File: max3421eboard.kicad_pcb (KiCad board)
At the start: 2 copper layers, 41.3 x 48.9 mm, 28 parts, among them J1 USB A, J2 USB MicroB, J3 1x10, J4 1x8, J5 1x8, J6 1x3, J7 Conn_01x04, U1 MAX3421E, U2 LP2985-3.3, U3 STMPS2141STR, Y1 12MHz

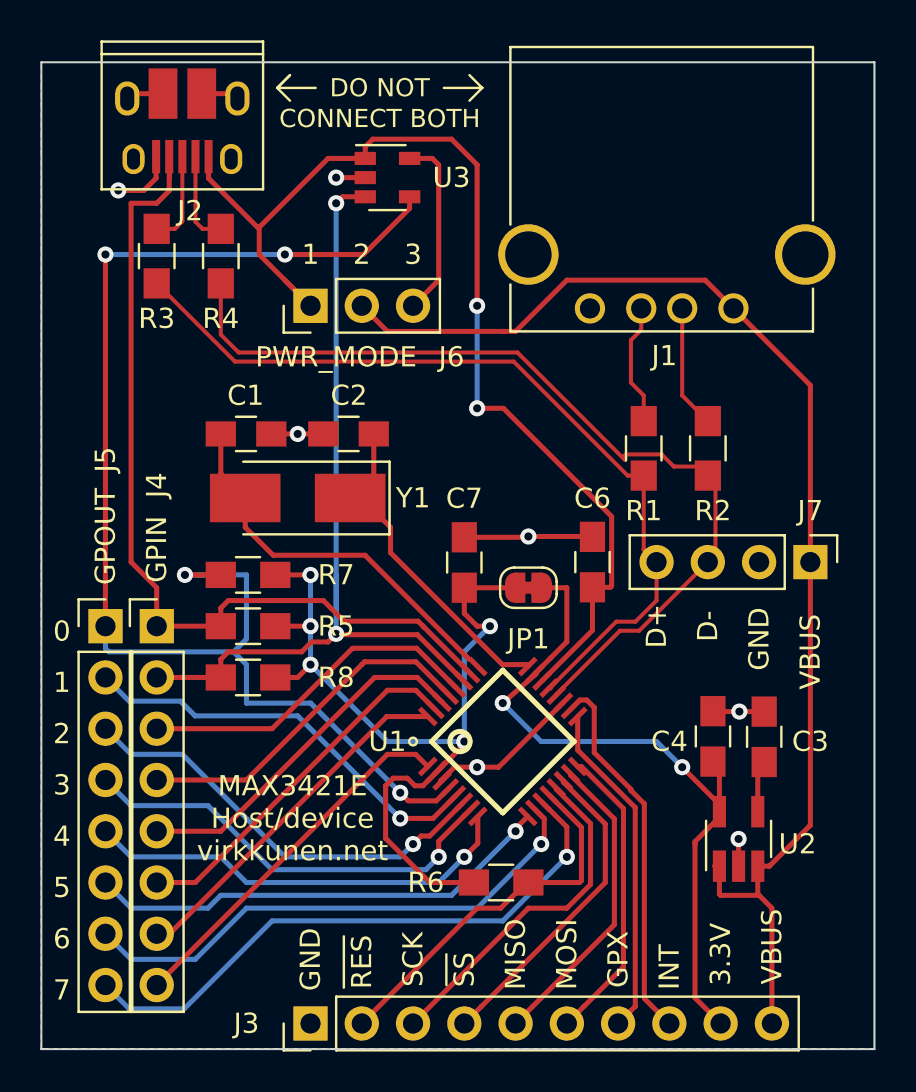
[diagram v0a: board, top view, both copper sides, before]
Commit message: Added more filtering/bypass and revised layout
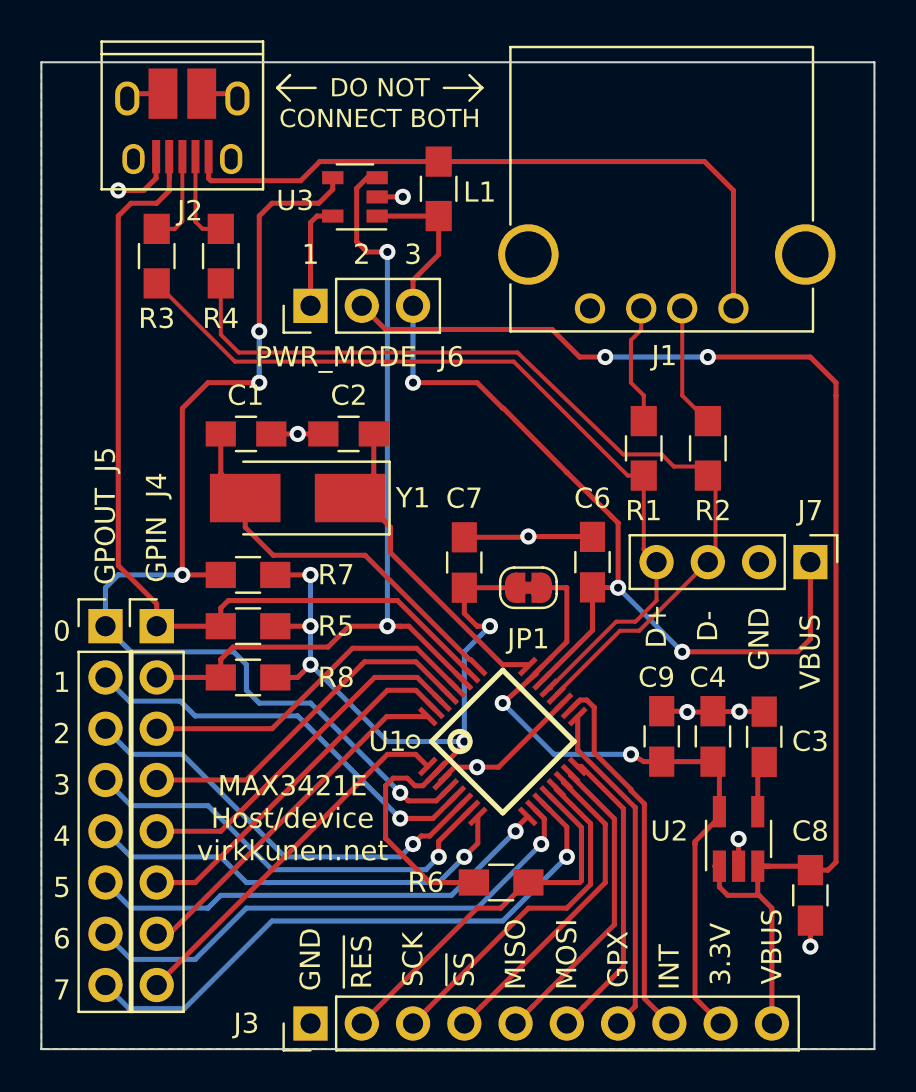
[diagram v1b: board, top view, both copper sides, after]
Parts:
- added C8: 1u, Capacitors_SMD:C_0805_HandSoldering, F.Cu at (55.9, 88.3)
- added C9: 100n, Capacitors_SMD:C_0805_HandSoldering, F.Cu at (48.5, 80.4)
- added L1: 120 @ 100MHz, Inductors_SMD:L_0805_HandSoldering, F.Cu at (37.5, 53.3)
- moved U3 1.87 mm to (33.3, 53.7), turned to 180 degrees
- moved REF*** 1.62 mm to (45.1, 66.7)
- moved G*** 0.14 mm to (42.5, 91.4)
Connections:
- J1 pad 1: VBUS -> Net-(J1-Pad1)
- J2 pad 1: Net-(C6-Pad1) -> Net-(J1-Pad1)
- J6 pad 1: Net-(C6-Pad1) -> Net-(J6-Pad1)
- J6 pad 3: Net-(J6-Pad3) -> Net-(C6-Pad1)
- J7 pad 1: VBUS -> Net-(C6-Pad1)
- U3 pad 5: Net-(J6-Pad3) -> Net-(J6-Pad1)
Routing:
- net Net-(J1-Pad1): track 0.00 -> 34.4 mm
- net /PWR_EN: track 66.5 -> 55.1 mm
- net Net-(J6-Pad3): track 9.08 -> 0.00 mm
- net Net-(C6-Pad1): track 57.1 -> 49.9 mm, vias 2 -> 3
- net Net-(J6-Pad1): track 0.00 -> 5.36 mm
- net GND: track 31.2 -> 34.9 mm, vias 7 -> 9
- net VBUS: track 63.1 -> 65.8 mm, vias 0 -> 2
- net +3V3: track 36.0 -> 35.0 mm
- net /PWR_FAULT: track 42.7 -> 41.9 mm

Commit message: Moved bypass caps closer to U1
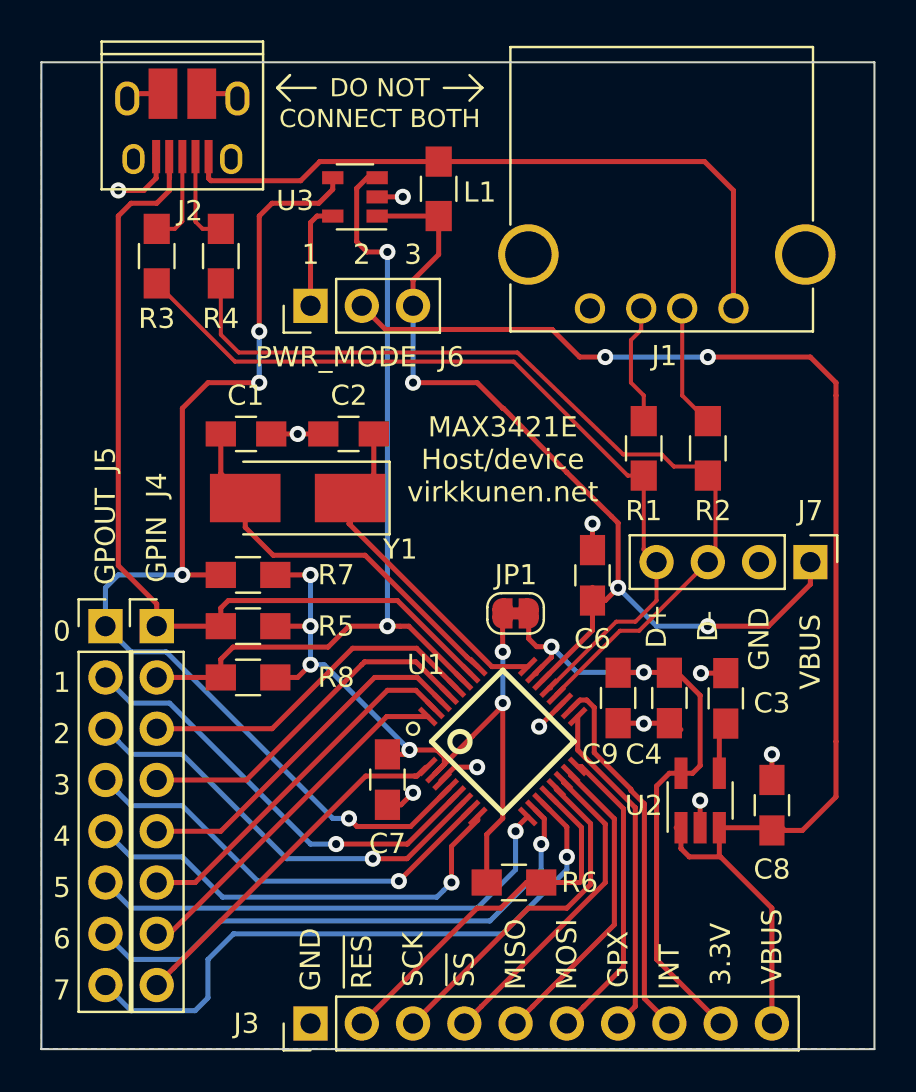
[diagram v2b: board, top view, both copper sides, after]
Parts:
- moved C7 11.4 mm to (34.9, 82.5), turned to 270 degrees
- moved C8 4.85 mm to (54.0, 83.8), turned to 90 degrees
- moved C9 2.88 mm to (46.4, 78.5), turned to 270 degrees
- moved C4 2.88 mm to (48.9, 78.5), turned to 270 degrees
- moved C3 2.69 mm to (51.7, 78.5)
- moved U2 2.69 mm to (50.4, 83.6)
- moved JP1 1.42 mm to (41.3, 74.3)
- moved C6 0.66 mm to (45.1, 72.4)
- moved R6 0.63 mm to (41.2, 87.6)
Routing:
- net GND: track 34.9 -> 26.4 mm, vias 9 -> 11
- net VL: track 44.5 -> 39.2 mm, vias 5 -> 6
- net Net-(C6-Pad1): track 49.9 -> 47.6 mm
- net Net-(J5-Pad8): track 29.7 -> 31.2 mm
- net +3V3: track 35.0 -> 33.8 mm
- net Net-(J5-Pad6): track 23.4 -> 24.5 mm
- net Net-(J5-Pad2): track 20.8 -> 21.8 mm
- net Net-(J5-Pad5): track 21.6 -> 22.6 mm
- net /PWR_EN: track 55.1 -> 56.1 mm
- net VBUS: track 65.8 -> 66.6 mm
- net Net-(J5-Pad7): track 26.5 -> 27.2 mm
- net Net-(J4-Pad8): track 18.4 -> 17.8 mm
- net /X-: track 17.8 -> 18.4 mm
- net /X+: track 19.9 -> 20.5 mm

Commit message: Add one more cap and move bypass around even more
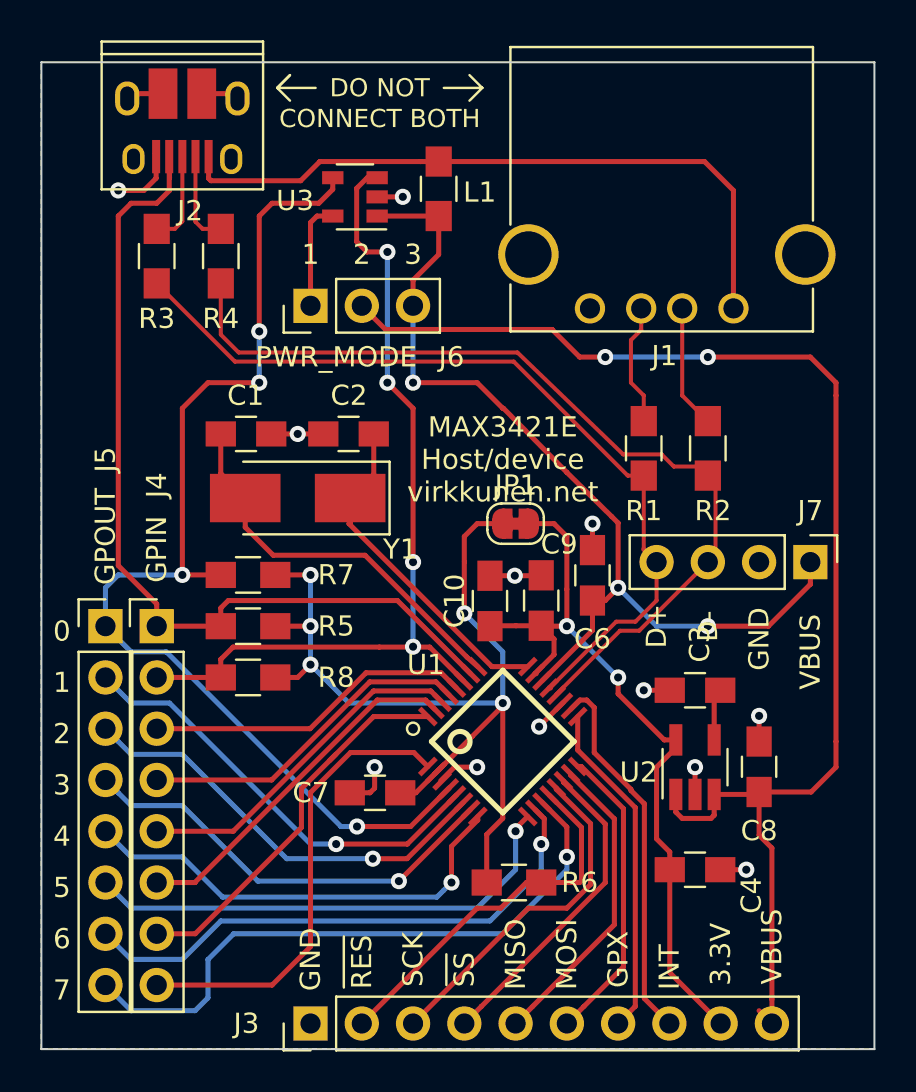
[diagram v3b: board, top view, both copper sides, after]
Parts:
- added C10: 1u, Capacitors_SMD:C_0805_HandSoldering, F.Cu at (40.0, 73.7)
- moved C4 8.60 mm to (50.2, 87.0), turned to 0 degrees
- moved C9 6.15 mm to (42.5, 73.7), turned to 90 degrees
- moved JP1 4.45 mm to (41.3, 69.8)
- moved C8 2.01 mm to (53.3, 81.9)
- moved U2 1.67 mm to (50.2, 81.9)
- moved C3 1.58 mm to (50.2, 78.1), turned to 180 degrees
- moved C7 0.90 mm to (34.3, 83.2), turned to 180 degrees
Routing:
- net VL: track 39.2 -> 48.2 mm, vias 6 -> 5
- net Net-(J4-Pad8): track 17.8 -> 23.0 mm
- net +3V3: track 33.8 -> 37.5 mm
- net Net-(J4-Pad7): track 17.3 -> 20.1 mm
- net GND: track 26.4 -> 28.1 mm, vias 11 -> 12
- net /PWR_FAULT: track 41.9 -> 43.0 mm, vias 2 -> 4
- net Net-(J4-Pad3): track 17.3 -> 16.3 mm
- net Net-(J4-Pad4): track 17.6 -> 16.8 mm
- net VBUS: track 66.6 -> 67.4 mm
- net Net-(C6-Pad1): track 47.6 -> 46.9 mm
- net Net-(J4-Pad5): track 17.8 -> 17.3 mm

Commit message: Layout clean-up
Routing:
- net /PWR_FAULT: track 43.0 -> 56.5 mm, vias 4 -> 3
- net /USB_ID: track 46.0 -> 43.6 mm, vias 0 -> 1
- net /PWR_EN: track 56.1 -> 54.2 mm, vias 4 -> 3

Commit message: Clean-up
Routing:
- net /X+: track 20.5 -> 21.4 mm
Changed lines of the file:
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@@
     (thickness 1.6)
     (drawings 47)
-    (tracks 460)
+    (tracks 458)
     (zones 0)
     (modules 32)
@@
   (segment (start 24.115 52.74) (end 22.235 54.62) (width 0.25) (layer F.Cu) (net 28))
   (segment (start 26.67 77.47) (end 23.495 77.47) (width 0.25) (layer F.Cu) (net 29))
-  (segment (start 38.695456 77.639796) (end 37.020659 75.964999) (width 0.25) (layer F.Cu) (net 29))
   (segment (start 26.67 76.57) (end 26.67 77.47) (width 0.25) (layer F.Cu) (net 29))
-  (segment (start 27.275001 75.964999) (end 26.67 76.57) (width 0.25) (layer F.Cu) (net 29))
-  (segment (start 34.525001 75.964999) (end 34.525001 75.964999) (width 0.25) (layer F.Cu) (net 29))
-  (segment (start 37.020659 75.964999) (end 34.525001 75.964999) (width 0.25) (layer F.Cu) (net 29))
-  (segment (start 34.525001 75.964999) (end 27.275001 75.964999) (width 0.25) (layer F.Cu) (net 29))
   (segment (start 32.385 62.865) (end 32.385 62.865) (width 0.25) (layer F.Cu) (net 29))
   (via (at 32.385 62.865) (size 0.8) (drill 0.4) (layers F.Cu B.Cu) (net 29))
@@
   (segment (start 28.136998 62.865) (end 28.226999 62.774999) (width 0.25) (layer F.Cu) (net 29))
   (segment (start 28.226999 62.774999) (end 29.119999 62.774999) (width 0.25) (layer F.Cu) (net 29))
+  (segment (start 26.67 76.57) (end 27.04 76.2) (width 0.25) (layer F.Cu) (net 29))
+  (segment (start 37.25566 76.2) (end 38.695456 77.639796) (width 0.25) (layer F.Cu) (net 29))
+  (segment (start 27.04 76.2) (end 37.25566 76.2) (width 0.25) (layer F.Cu) (net 29))
   (segment (start 32.217 53.285) (end 31.527 53.975) (width 0.25) (layer F.Cu) (net 30))
   (segment (start 32.217 52.71) (end 32.217 53.285) (width 0.25) (layer F.Cu) (net 30))
@@
   (segment (start 29.37 74.93) (end 29.845 74.93) (width 0.25) (layer F.Cu) (net 31))
   (segment (start 29.845 74.93) (end 31.115 74.93) (width 0.25) (layer F.Cu) (net 31))
-  (segment (start 29.37 77.47) (end 30.48 77.47) (width 0.25) (layer F.Cu) (net 31))
-  (segment (start 30.48 77.47) (end 31.115 76.835) (width 0.25) (layer F.Cu) (net 31))
-  (segment (start 31.115 76.835) (end 31.115 76.835) (width 0.25) (layer F.Cu) (net 31))
-  (via (at 31.115 76.835) (size 0.8) (drill 0.4) (layers F.Cu B.Cu) (net 31))
+  (via (at 31.115 77.47) (size 0.8) (drill 0.4) (layers F.Cu B.Cu) (net 31))
   (segment (start 31.115 74.93) (end 31.115 74.93) (width 0.25) (layer F.Cu) (net 31))
   (via (at 31.115 74.93) (size 0.8) (drill 0.4) (layers F.Cu B.Cu) (net 31))
@@
   (segment (start 40.64 76.2) (end 40.64 78.74) (width 0.25) (layer B.Cu) (net 31))
   (segment (start 38.735 74.295) (end 38.735 74.295) (width 0.25) (layer B.Cu) (net 31))
-  (segment (start 31.115 76.835) (end 33.02 78.74) (width 0.25) (layer B.Cu) (net 31))
   (segment (start 33.02 78.74) (end 40.64 78.74) (width 0.25) (layer B.Cu) (net 31))
   (segment (start 38.735 74.295) (end 40.64 76.2) (width 0.25) (layer B.Cu) (net 31))
@@
   (segment (start 39.37 69.85) (end 38.735 70.485) (width 0.25) (layer F.Cu) (net 31))
   (segment (start 40.625 69.85) (end 39.37 69.85) (width 0.25) (layer F.Cu) (net 31))
+  (segment (start 29.37 77.47) (end 31.115 77.47) (width 0.25) (layer F.Cu) (net 31))
+  (segment (start 31.115 76.835) (end 31.115 77.47) (width 0.25) (layer B.Cu) (net 31))
+  (segment (start 31.115 77.47) (end 32.385 78.74) (width 0.25) (layer B.Cu) (net 31))
+  (segment (start 32.385 78.74) (end 33.02 78.74) (width 0.25) (layer B.Cu) (net 31))
   (segment (start 47.625 67.47) (end 47.625 71.12) (width 0.2) (layer F.Cu) (net 32))
   (segment (start 42.938097 77.99335) (end 43.005963 77.99335) (width 0.25) (layer F.Cu) (net 32))
@@
   (segment (start 26.67 67.37) (end 27.88 68.58) (width 0.25) (layer F.Cu) (net 34))
   (segment (start 26.67 65.405) (end 26.67 67.37) (width 0.25) (layer F.Cu) (net 34))
-  (segment (start 33.817006 71.414999) (end 38.869326 76.467319) (width 0.25) (layer F.Cu) (net 34))
-  (segment (start 29.264999 71.414999) (end 33.817006 71.414999) (width 0.25) (layer F.Cu) (net 34))
-  (segment (start 27.88 68.58) (end 27.88 70.03) (width 0.25) (layer F.Cu) (net 34))
   (segment (start 38.869326 76.467319) (end 39.402563 76.932689) (width 0.25) (layer F.Cu) (net 34))
-  (segment (start 27.88 70.03) (end 29.264999 71.414999) (width 0.25) (layer F.Cu) (net 34))
+  (segment (start 27.88 68.58) (end 27.88 70.425) (width 0.25) (layer F.Cu) (net 34))
+  (segment (start 27.88 70.425) (end 28.575 71.12) (width 0.25) (layer F.Cu) (net 34))
+  (segment (start 33.589874 71.12) (end 39.402563 76.932689) (width 0.25) (layer F.Cu) (net 34))
+  (segment (start 28.575 71.12) (end 33.589874 71.12) (width 0.25) (layer F.Cu) (net 34))
   (segment (start 33.02 68.52) (end 33.08 68.58) (width 0.25) (layer F.Cu) (net 35))
   (segment (start 32.385 67.885) (end 33.08 68.58) (width 0.25) (layer F.Cu) (net 35))
